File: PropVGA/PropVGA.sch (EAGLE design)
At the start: 10 parts

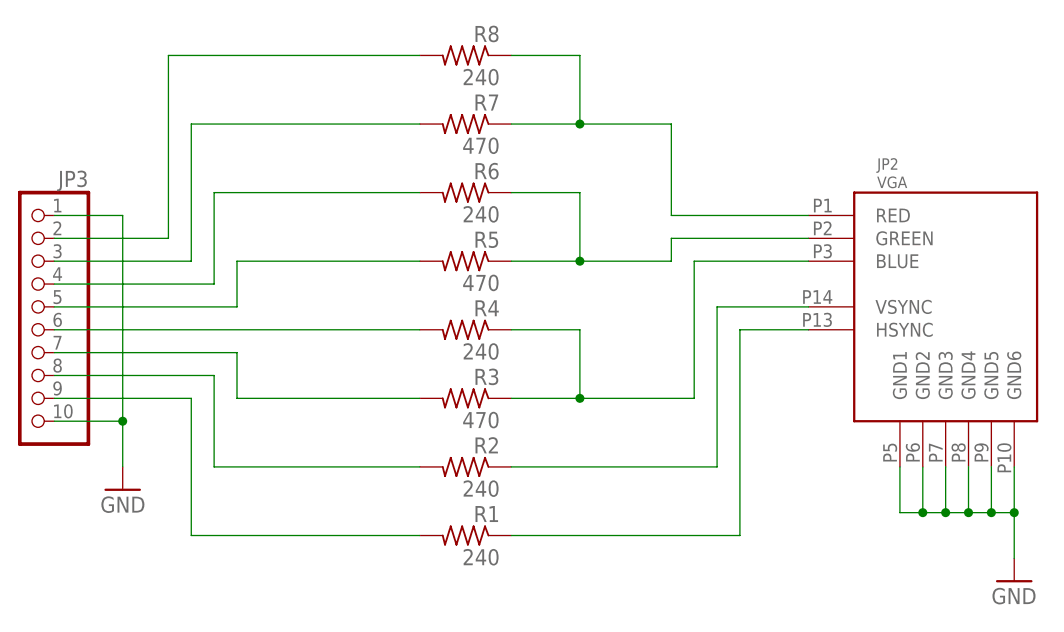
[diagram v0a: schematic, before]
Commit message: Corrected HSYNC / VSYNC connections
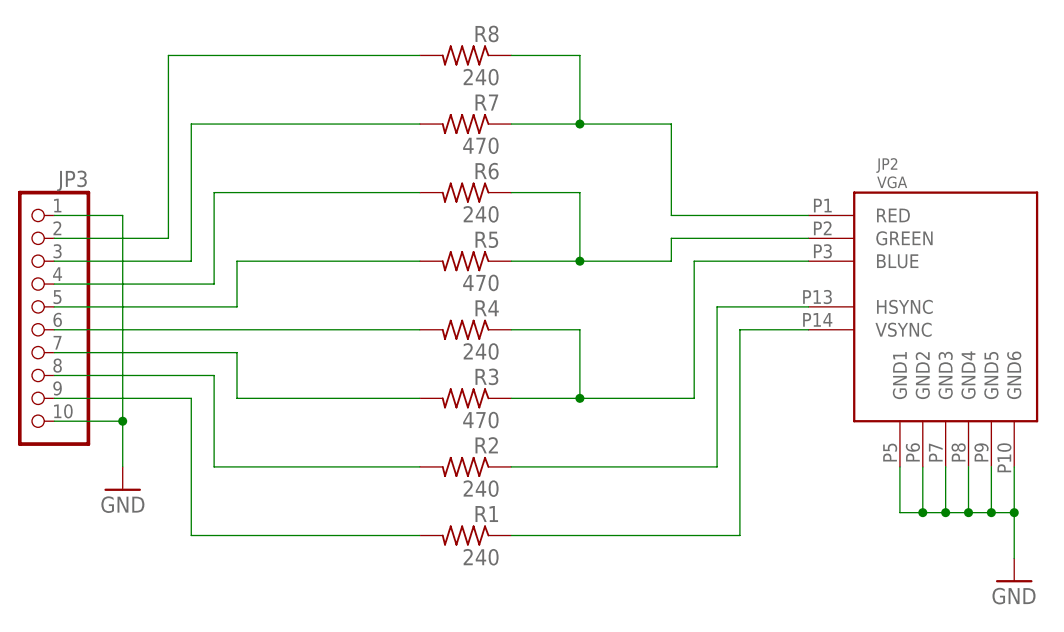
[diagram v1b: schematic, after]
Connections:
- net H: now also JP2.HSYNC; no longer JP2.VSYNC
- net V: now also JP2.VSYNC; no longer JP2.HSYNC
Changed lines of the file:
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@@
 <wire x1="147.32" y1="99.06" x2="147.32" y2="76.2" width="0.1524" layer="91"/>
 <wire x1="147.32" y1="76.2" x2="121.92" y2="76.2" width="0.1524" layer="91"/>
-<pinref part="JP2" gate="JP$1" pin="HSYNC"/>
+<pinref part="JP2" gate="JP$1" pin="VSYNC"/>
 </segment>
 </net>
@@
 <wire x1="144.78" y1="101.6" x2="144.78" y2="83.82" width="0.1524" layer="91"/>
 <wire x1="144.78" y1="83.82" x2="121.92" y2="83.82" width="0.1524" layer="91"/>
-<pinref part="JP2" gate="JP$1" pin="VSYNC"/>
+<pinref part="JP2" gate="JP$1" pin="HSYNC"/>
 </segment>
 </net>
